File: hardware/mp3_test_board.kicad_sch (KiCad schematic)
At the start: 0 parts

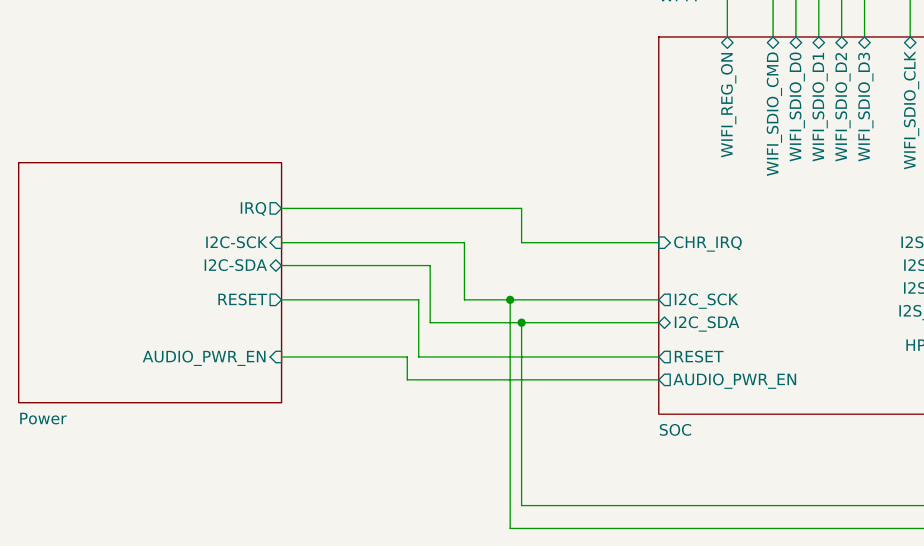
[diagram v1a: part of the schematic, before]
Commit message: pwr btn is optional connected to soc
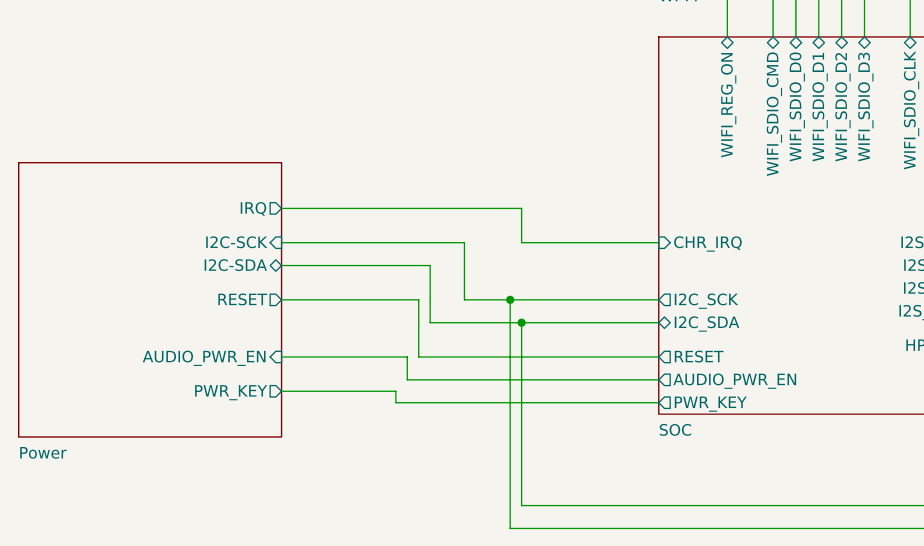
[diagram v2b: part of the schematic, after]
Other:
- sheet Power ports: added PWR_KEY; removed none
- sheet SOC ports: added PWR_KEY; removed none
